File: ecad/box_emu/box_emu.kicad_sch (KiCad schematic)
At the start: 4 parts

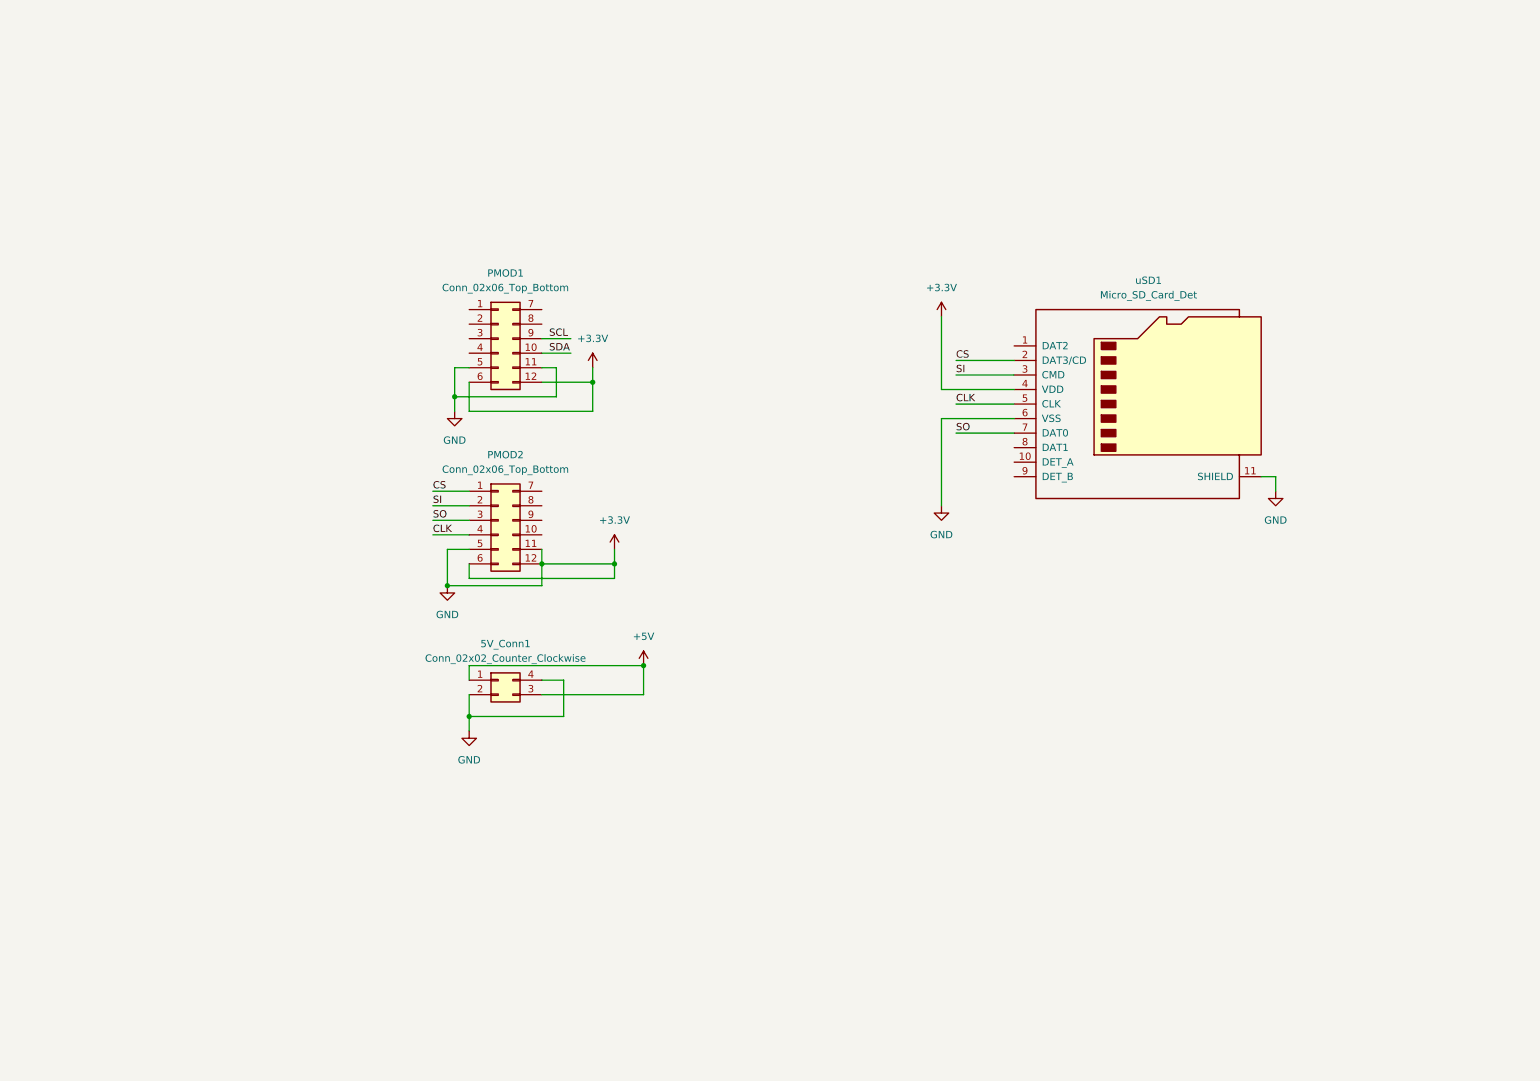
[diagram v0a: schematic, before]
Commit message: WIP fleshing out schematic for esp box emu pcb; added usb c port, mcp23017, ads1015, drv2605, battery charger, etc.
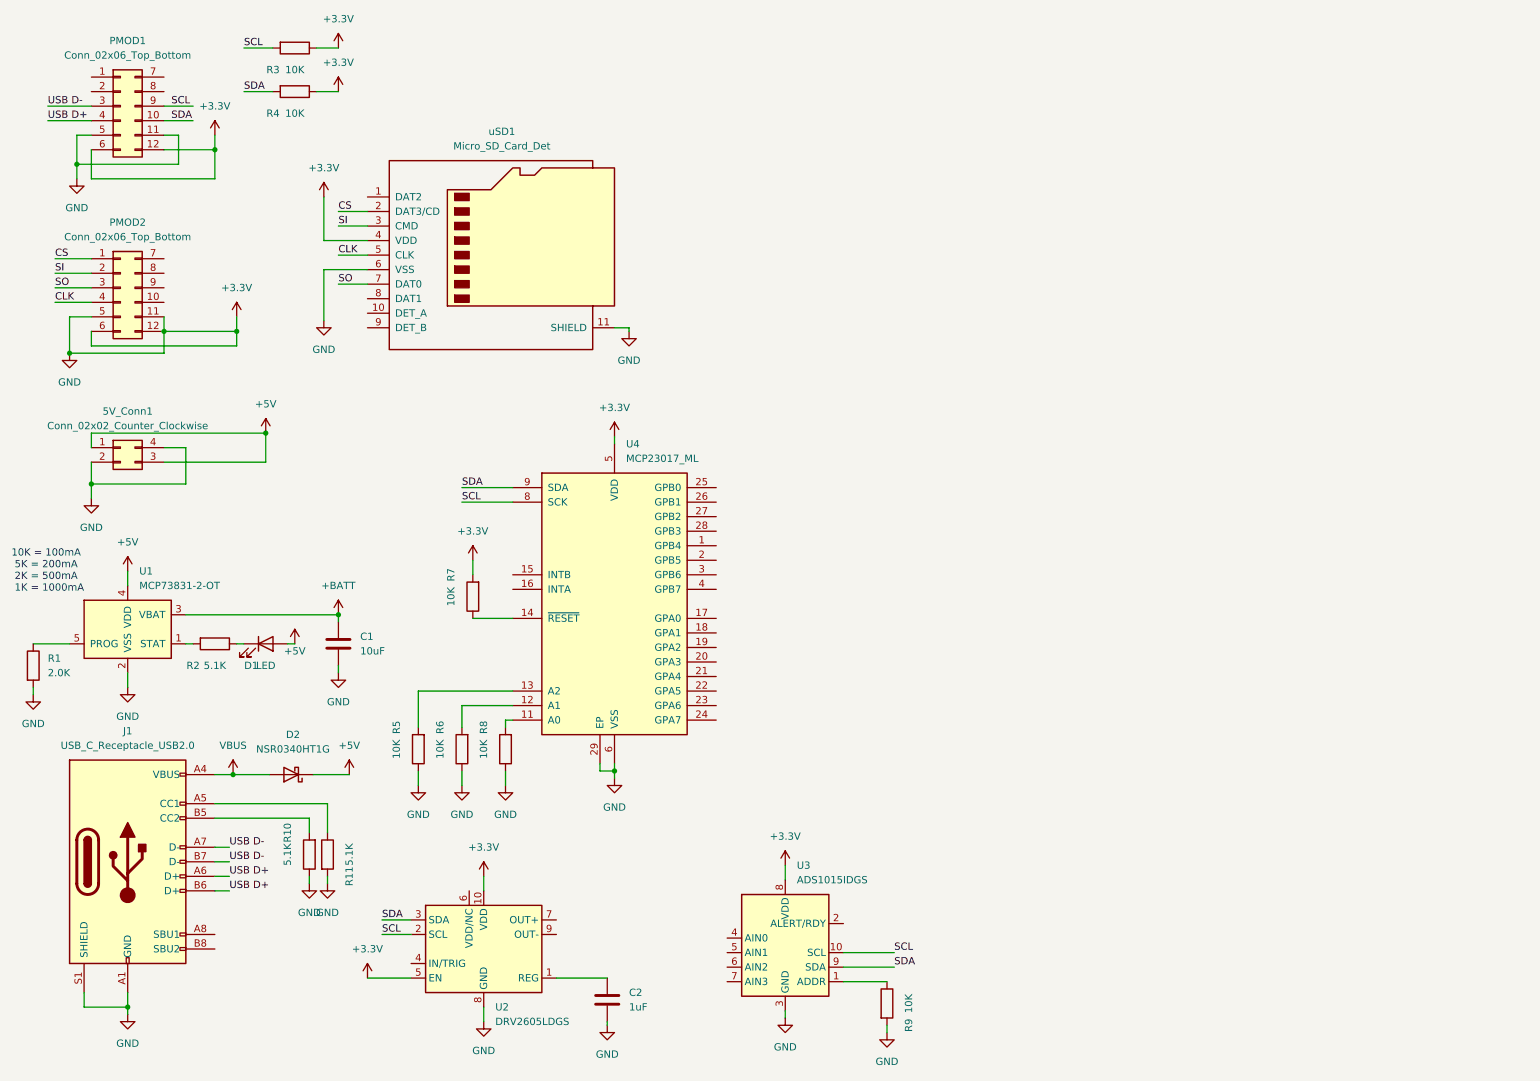
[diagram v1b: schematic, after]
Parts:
- added C1: 10uF, symbol Device:C
- added C2: 1uF, Capacitor_SMD:C_0603_1608Metric_Pad1.08x0.95mm_HandSolder, symbol Device:C
- added D1: LED, symbol Device:LED
- added D2: NSR0340HT1G, Diode_SMD:D_SOD-323, symbol Diode:NSR0340HT1G
- added J1: USB_C_Receptacle_USB2.0, symbol Connector:USB_C_Receptacle_USB2.0
- added R1: 2.0K, Resistor_SMD:R_0402_1005Metric_Pad0.72x0.64mm_HandSolder, symbol Device:R
- added R10, R11, R2: 5.1K, Resistor_SMD:R_0402_1005Metric_Pad0.72x0.64mm_HandSolder, symbol Device:R
- added R3, R4, R5, R6, R7, R8, R9: 10K, Resistor_SMD:R_0402_1005Metric_Pad0.72x0.64mm_HandSolder, symbol Device:R
- added U1: MCP73831-2-OT, Package_TO_SOT_SMD:SOT-23-5, symbol Battery_Management:MCP73831-2-OT
- added U2: DRV2605LDGS, Package_SO:VSSOP-10_3x3mm_P0.5mm, symbol Driver_Haptic:DRV2605LDGS
- added U3: ADS1015IDGS, Package_SO:TSSOP-10_3x3mm_P0.5mm, symbol Analog_ADC:ADS1015IDGS
- added U4: MCP23017_ML, Package_DFN_QFN:QFN-28-1EP_6x6mm_P0.65mm_EP4.25x4.25mm, symbol Interface_Expansion:MCP23017_ML
- 5V_Conn1: footprint (none) -> Connector_PinHeader_2.54mm:PinHeader_2x02_P2.54mm_Horizontal
- PMOD1, PMOD2: footprint (none) -> Connector_PinHeader_2.54mm:PinHeader_2x06_P2.54mm_Horizontal
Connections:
- net +3.3V: now also C1.2, C2.2, J1.A1 (GND), J1.A12 (GND), J1.B1 (GND), J1.B12 (GND), J1.S1 (SHIELD), R1.2, R10.1, R11.2, R3.1, R4.1, R5.1, R6.1, R7.2, R8.1, R9.2, U1.2 (VSS), U2.10 (VDD), U2.5 (EN), U2.8 (GND), U3.3 (GND), U3.8 (VDD), U4.29 (EP), U4.5 (VDD), U4.6 (VSS)
- net +5V: now also D1.2 (A), D2.1 (K), U1.4 (VDD)
- net SCL: now also R3.2, U2.2 (SCL), U3.10 (SCL), U4.8 (SCK)
- net SDA: now also R4.2, U2.3 (SDA), U3.9 (SDA), U4.9 (SDA)
- net USB D-: now reaches PMOD1.3 (Pin_3)
- net USB D-: now also J1.A7 (D-), J1.B7 (D-)
- net USB D+: now reaches PMOD1.4 (Pin_4)
- net USB D+: now also J1.A6 (D+), J1.B6 (D+)
- new net: R9.1, U3.1 (ADDR)
- new net: D1.1 (K), R2.1
- new net: R8.2, U4.11 (A0)
- new net: R7.1, U4.14 (~{RESET})
- new net: R2.2, U1.1 (STAT)
- new net: C2.1, U2.1 (REG)
- new net: J1.A5 (CC1), R11.1
- new net: J1.B5 (CC2), R10.2
- new net: R5.2, U4.13 (A2)
- new net: R6.2, U4.12 (A1)
- new net: R1.1, U1.5 (PROG)
- new net +BATT: C1.1, U1.3 (VBAT)
- new net VBUS: D2.2 (A), J1.A4 (VBUS), J1.A9 (VBUS), J1.B4 (VBUS), J1.B9 (VBUS)
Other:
- note added: "10K = 100mA 5K = 200mA 2K = 500mA 1K = 1000mA"
- moved on the sheet: 5V_Conn1, PMOD1, PMOD2, uSD1

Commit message: WIP fleshing out ecad some more - added buttons, 5v boost converter, and moved some things around.
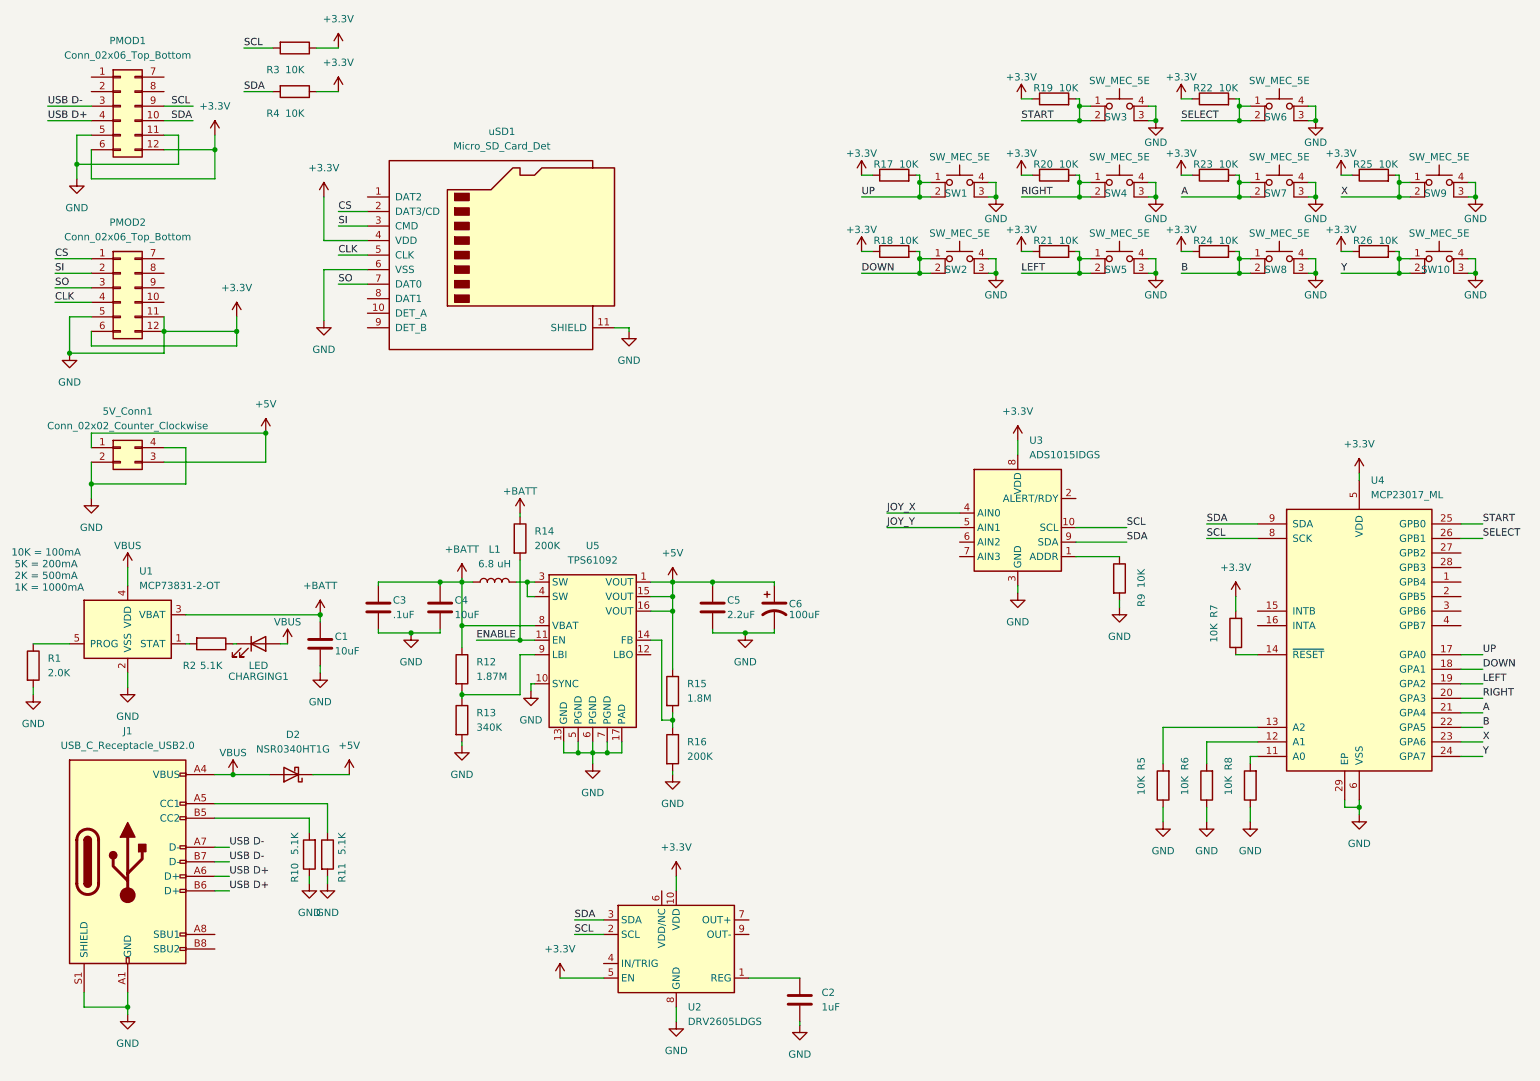
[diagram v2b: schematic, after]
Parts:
- added C3: .1uF, Capacitor_SMD:C_0603_1608Metric_Pad1.08x0.95mm_HandSolder, symbol Device:C
- added C4: 10uF, Capacitor_SMD:C_0603_1608Metric_Pad1.08x0.95mm_HandSolder, symbol Device:C
- added C5: 2.2uF, Capacitor_SMD:C_0603_1608Metric_Pad1.08x0.95mm_HandSolder, symbol Device:C
- added C6: 100uF, symbol Device:C_Polarized_US
- added L1: 6.8 uH, symbol Device:L
- added R12: 1.87M, Resistor_SMD:R_0402_1005Metric_Pad0.72x0.64mm_HandSolder, symbol Device:R
- added R13: 340K, Resistor_SMD:R_0402_1005Metric_Pad0.72x0.64mm_HandSolder, symbol Device:R
- added R14, R16: 200K, Resistor_SMD:R_0402_1005Metric_Pad0.72x0.64mm_HandSolder, symbol Device:R
- added R15: 1.8M, Resistor_SMD:R_0402_1005Metric_Pad0.72x0.64mm_HandSolder, symbol Device:R
- added R17, R18, R19, R20, R21, R22, R23, R24, R25, R26: 10K, Resistor_SMD:R_0402_1005Metric_Pad0.72x0.64mm_HandSolder, symbol Device:R
- added SW1, SW10, SW2, SW3, SW4, SW5, SW6, SW7, SW8, SW9: SW_MEC_5E, symbol Switch:SW_MEC_5E
- added U5: TPS61092, Package_DFN_QFN:Texas_S-PVQFN-N16_EP2.7x2.7mm_ThermalVias, symbol Regulator_Switching:TPS61092
- C1: footprint (none) -> Capacitor_SMD:C_0603_1608Metric_Pad1.08x0.95mm_HandSolder
- CHARGING1: renamed from D1; footprint (none) -> LED_SMD:LED_1812_4532Metric_Pad1.30x3.40mm_HandSolder
- J1: footprint (none) -> Connector_USB:USB_C_Plug_Molex_105444
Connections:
- net +3.3V: now also C3.2, C4.2, C5.2, C6.2, R13.2, R16.2, R17.1, R18.1, R19.1, R20.1, R21.1, R22.1, R23.1, R24.1, R25.1, R26.1, SW1.3 (K), SW1.4 (A), SW10.3 (K), SW10.4 (A), SW2.3 (K), SW2.4 (A), SW3.3 (K), SW3.4 (A), SW4.3 (K), SW4.4 (A), SW5.3 (K), SW5.4 (A), SW6.3 (K), SW6.4 (A), SW7.3 (K), SW7.4 (A), SW8.3 (K), SW8.4 (A), SW9.3 (K), SW9.4 (A), U5.10 (SYNC), U5.13 (GND), U5.17 (PAD), U5.5 (PGND), U5.6 (PGND), U5.7 (PGND)
- net +5V: now also C5.1, C6.1, R15.1, U5.1 (VOUT), U5.15 (VOUT), U5.16 (VOUT); no longer CHARGING1.2 (A), U1.4 (VDD)
- net +BATT: now also C3.1, C4.1, L1.1, R12.1, R14.1, U5.8 (VBAT)
- net VBUS: now also CHARGING1.2 (A), U1.4 (VDD)
- net JOY_X: now reaches U3.4 (AIN0)
- net JOY_Y: now reaches U3.5 (AIN1)
- net UP: now reaches U4.17 (GPA0)
- net UP: now also R17.2, SW1.1, SW1.2
- net DOWN: now reaches U4.18 (GPA1)
- net DOWN: now also R18.2, SW2.1, SW2.2
- net LEFT: now reaches U4.19 (GPA2)
- net LEFT: now also R21.2, SW5.1, SW5.2
- net RIGHT: now reaches U4.20 (GPA3)
- net RIGHT: now also R20.2, SW4.1, SW4.2
- net A: now reaches U4.21 (GPA4)
- net A: now also R23.2, SW7.1, SW7.2
- net B: now reaches U4.22 (GPA5)
- net B: now also R24.2, SW8.1, SW8.2
- net X: now reaches U4.23 (GPA6)
- net X: now also R25.2, SW9.1, SW9.2
- net Y: now reaches U4.24 (GPA7)
- net Y: now also R26.2, SW10.1, SW10.2
- net START: now reaches U4.25 (GPB0)
- net START: now also R19.2, SW3.1, SW3.2
- net SELECT: now reaches U4.26 (GPB1)
- net SELECT: now also R22.2, SW6.1, SW6.2
- new net: L1.2, U5.3 (SW), U5.4 (SW)
- new net: R12.2, R13.1, U5.9 (LBI)
- new net: R15.2, R16.1, U5.14 (FB)
- new net ENABLE: R14.2, U5.11 (EN)
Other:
- moved on the sheet: C1, C2, CHARGING1, R2, R5, R6, R7, R8, R9, U2, U3, U4
